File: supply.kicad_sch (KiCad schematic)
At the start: 94 parts, among them J12 PJ-102A, Q12 BSS138W-7-F, Q13 BCM857BS-7-F, Q14 BCM857BS-7-F, Q15 SSM3J332R, Q16 SSM3J332R, Q17 BSS138W-7-F, Q18 BSS138W-7-F, Q19 BSS138W-7-F, Q20 BSS138W-7-F, SW1 PCM12SMTR, U35 RB521S30T1G, U36 RB521S30T1G, U37 74LVC2G14GV, U38 74LVC1G175GV, U39 MP2386GG-P, U40 MP2386GG-P, U41 TPS7B8133DRVR, U42 TPS7A0518PDBVT

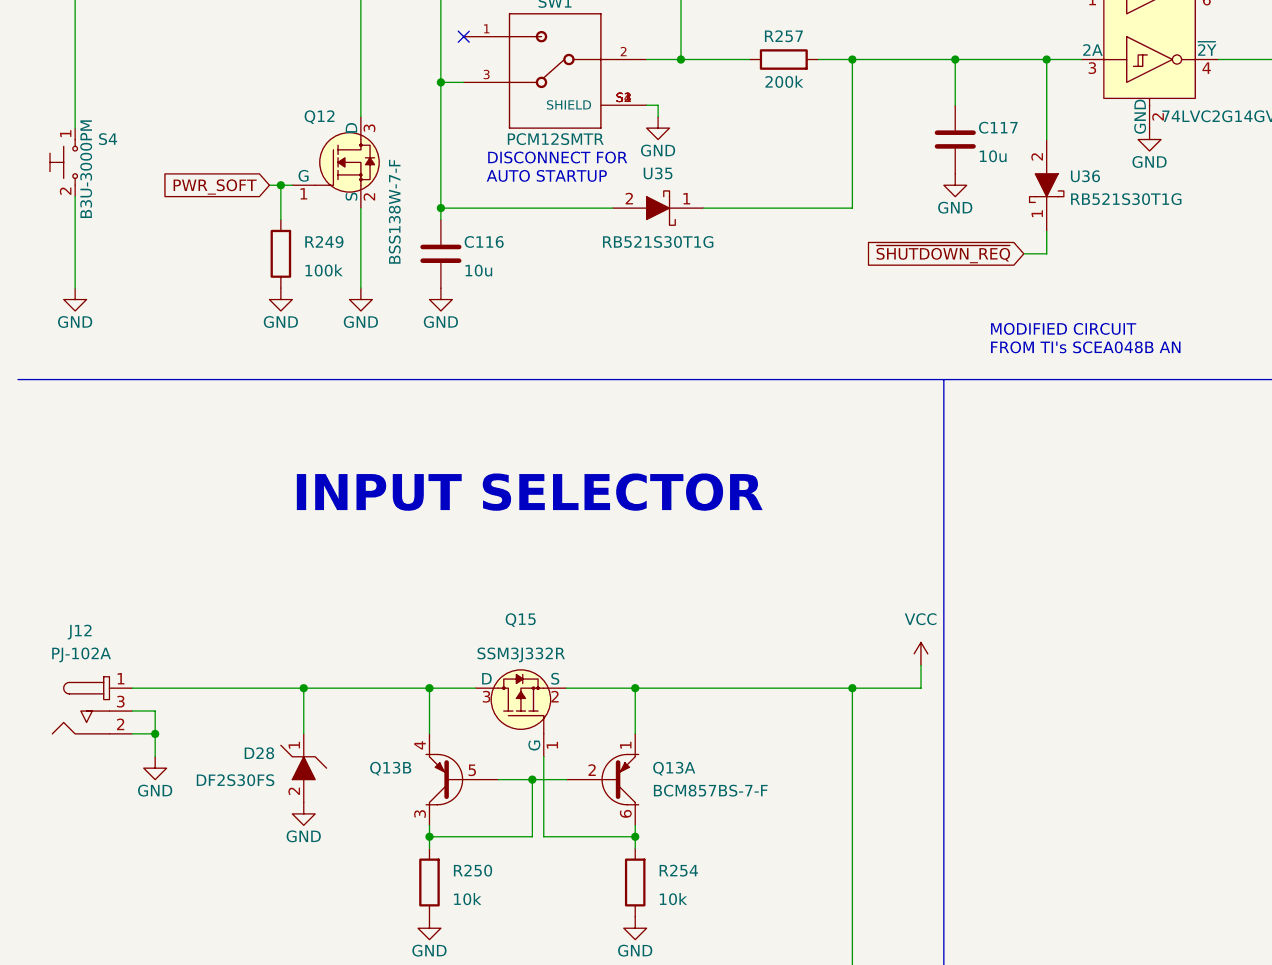
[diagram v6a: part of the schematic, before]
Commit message: Update RB521S30T1G symbol and footprint
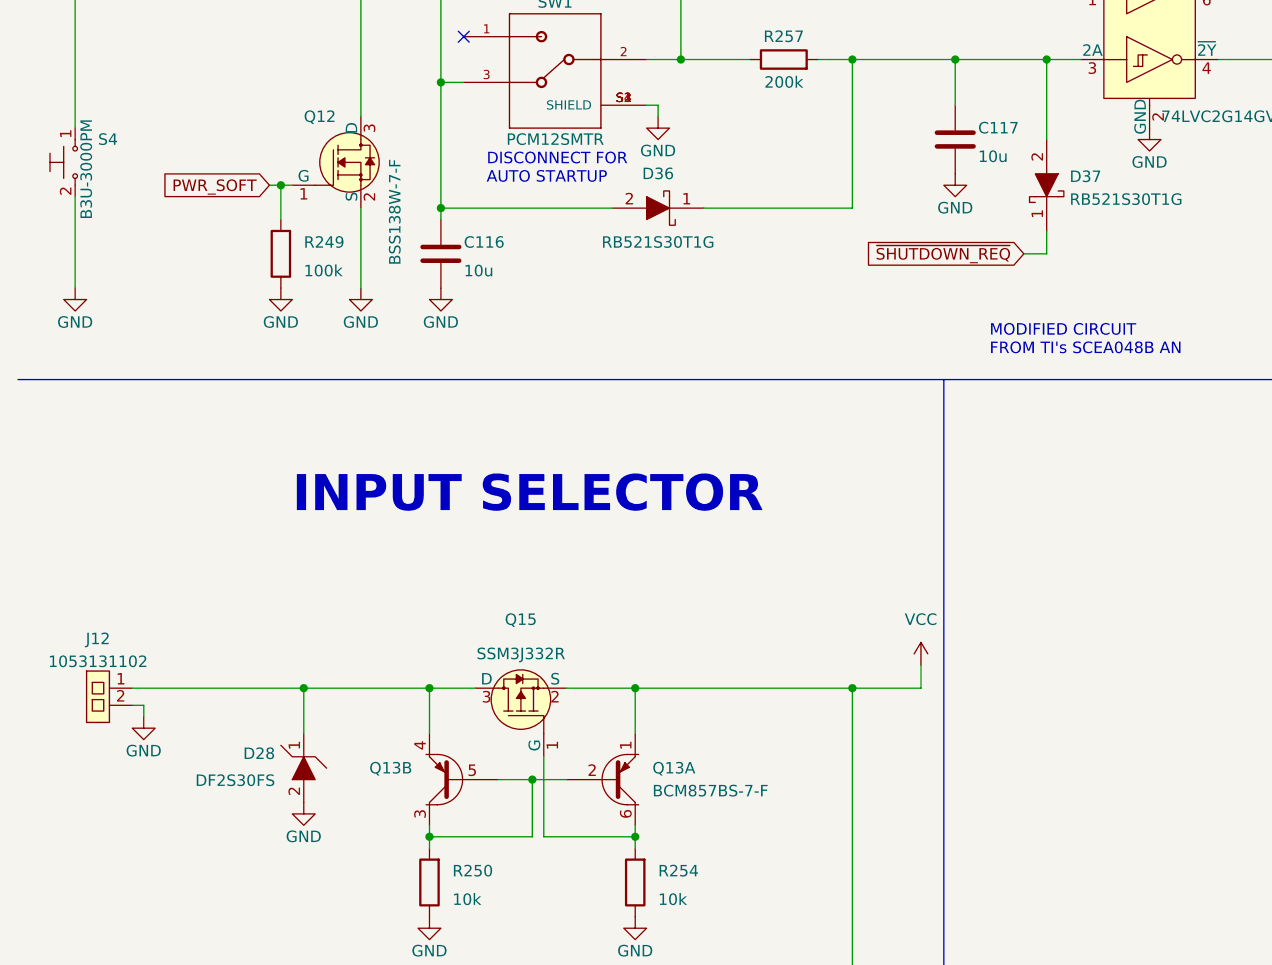
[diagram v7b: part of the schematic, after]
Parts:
- removed J12: PJ-102A, antmicro-footprints:Barrel_Jack_5.5mmODx2.1mmID_PJ-102A, symbol antmicroBarrelPowerConnectors:PJ-102A
- added J12: 1053131102, antmicro-footprints:1053131102, symbol antmicroRectangularConnectorsHeadersFemalePins:1053131102
- renumbered U35 to D36, U36 to D37
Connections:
- net GND: now also J12.2
- net at D28.1, Q13.4, Q15.3 (D): now also J12.1
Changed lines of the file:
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@@
   (junction (at 249.555 127) (diameter 0) (color 0 0 0 0)
   )
-  (junction (at 27.94 134.62) (diameter 0) (color 0 0 0 0)
-  )
   (junction (at 363.855 139.7) (diameter 0) (color 0 0 0 0)
   )
@@
     (stroke (width 0) (type default) (color 0 0 0 0))
   )
-  (wire (pts (xy 27.94 132.08) (xy 27.94 134.62))
-    (stroke (width 0) (type default) (color 0 0 0 0))
-  )
   (wire (pts (xy 86.36 46.99) (xy 86.36 59.69))
     (stroke (width 0) (type default) (color 0 0 0 0))
@@
     (stroke (width 0) (type default) (color 0 0 0 0))
   )
-  (wire (pts (xy 25.4 132.08) (xy 27.94 132.08))
+  (wire (pts (xy 25.4 131.445) (xy 26.67 131.445))
     (stroke (width 0) (type default) (color 0 0 0 0))
   )
@@
     (stroke (width 0) (type default) (color 0 0 0 0))
   )
-  (wire (pts (xy 27.94 134.62) (xy 25.4 134.62))
-    (stroke (width 0) (type default) (color 0 0 0 0))
-  )
   (wire (pts (xy 236.22 127) (xy 249.555 127))
     (stroke (width 0) (type default) (color 0 0 0 0))
@@
     (stroke (width 0) (type default) (color 0 0 0 0))
   )
-  (wire (pts (xy 27.94 134.62) (xy 27.94 137.16))
+  (wire (pts (xy 26.67 131.445) (xy 26.67 132.715))
     (stroke (width 0) (type default) (color 0 0 0 0))
   )
@@
     (pin "6")
   )
-  (symbol (lib_id "antmicroDiodesRectifiersSingle:RB521S30T1G") (at 127 73.66 270) (unit 1)
+  (symbol (lib_name "RB521S30T1G_1") (lib_id "antmicroDiodesRectifiersSingle:RB521S30T1G") (at 127 73.66 270) (unit 1)
     (in_bom yes) (on_board yes) (fields_autoplaced)
-    (property "Reference" "U36" (id 0) (at 129.54 72.7074 90)
+    (property "Reference" "D37" (id 0) (at 129.54 72.7074 90)
       (effects (font (size 1.27 1.27)) (justify left))
     )
@@
   (symbol (lib_id "antmicroDiodesRectifiersSingle:RB521S30T1G") (at 83.82 76.2 0) (unit 1)
     (in_bom yes) (on_board yes)
-    (property "Reference" "U35" (id 0) (at 83.82 72.39 0))
+    (property "Reference" "D36" (id 0) (at 83.82 72.39 0))
     (property "Value" "RB521S30T1G" (id 1) (at 83.82 80.01 0))
     (property "Footprint" "antmicro-footprints:SOD-523" (id 2) (at 86.36 83.82 0)
@@
     (pin "2")
   )
-  (symbol (lib_id "power:GND") (at 27.94 137.16 0) (unit 1)
+  (symbol (lib_id "power:GND") (at 26.67 132.715 0) (unit 1)
     (in_bom yes) (on_board yes)
-    (property "Reference" "#PWR0250" (id 0) (at 27.94 143.51 0)
+    (property "Reference" "#PWR0250" (id 0) (at 26.67 139.065 0)
       (effects (font (size 1.27 1.27)) hide)
     )
-    (property "Value" "GND" (id 1) (at 27.94 140.97 0))
-    (property "Footprint" "" (id 2) (at 27.94 137.16 0)
+    (property "Value" "GND" (id 1) (at 26.67 136.525 0))
+    (property "Footprint" "" (id 2) (at 26.67 132.715 0)
       (effects (font (size 1.27 1.27)) hide)
     )
-    (property "Datasheet" "" (id 3) (at 27.94 137.16 0)
+    (property "Datasheet" "" (id 3) (at 26.67 132.715 0)
       (effects (font (size 1.27 1.27)) hide)
     )
@@
     (pin "1")
   )
-  (symbol (lib_id "antmicroBarrelPowerConnectors:PJ-102A") (at 22.86 129.54 0) (unit 1)
-    (in_bom yes) (on_board yes) (fields_autoplaced)
-    (property "Reference" "J12" (id 0) (at 19.685 123.19 0))
-    (property "Value" "PJ-102A" (id 1) (at 19.685 125.73 0))
-    (property "Footprint" "antmicro-footprints:Barrel_Jack_5.5mmODx2.1mmID_PJ-102A" (id 2) (at 27.94 124.46 0)
-      (effects (font (size 1.524 1.524)) (justify left) hide)
-    )
-    (property "Datasheet" "https://www.cui.com/product/resource/digikeypdf/pj-102a.pdf" (id 3) (at 27.94 121.92 0)
-      (effects (font (size 1.524 1.524)) (justify left) hide)
-    )
-    (property "Manufacturer" "CUI Inc." (id 4) (at 27.94 101.6 0)
-      (effects (font (size 1.524 1.524)) (justify left) hide)
-    )
-    (property "MPN" "PJ-102A" (id 5) (at 27.94 116.84 0)
-      (effects (font (size 1.524 1.524)) (justify left) hide)
-    )
-    (pin "1")
-    (pin "2")
-    (pin "3")
-  )
   (symbol (lib_id "antmicroCapacitorsmisc:C_22u_0805_25V") (at 222.885 132.08 0) (unit 1)
     (in_bom yes) (on_board yes) (fields_autoplaced)
@@
     )
     (pin "1")
+    (pin "2")
+  )
+  (symbol (lib_id "antmicroRectangularConnectorsHeadersFemalePins:1053131102") (at 20.32 127.635 0) (unit 1)
+    (in_bom yes) (on_board yes) (fields_autoplaced)
+    (property "Reference" "J12" (id 0) (at 21.59 124.0622 0))
+    (property "Value" "1053131102" (id 1) (at 21.59 126.5991 0))
+    (property "Footprint" "antmicro-footprints:1053131102" (id 2) (at 15.875 135.89 0)
+      (effects (font (size 1.27 1.27)) hide)
+    )
+    (property "Datasheet" "" (id 3) (at 20.32 127.635 0)
+      (effects (font (size 1.27 1.27)) hide)
+    )
+    (property "Manufacturer" "Molex" (id 4) (at 19.05 140.97 0)
+      (effects (font (size 1.27 1.27)) hide)
+    )
+    (property "MPN" "1053131102" (id 5) (at 17.145 139.065 0)
+      (effects (font (size 1.27 1.27)) hide)
+    )
+    (pin "1")

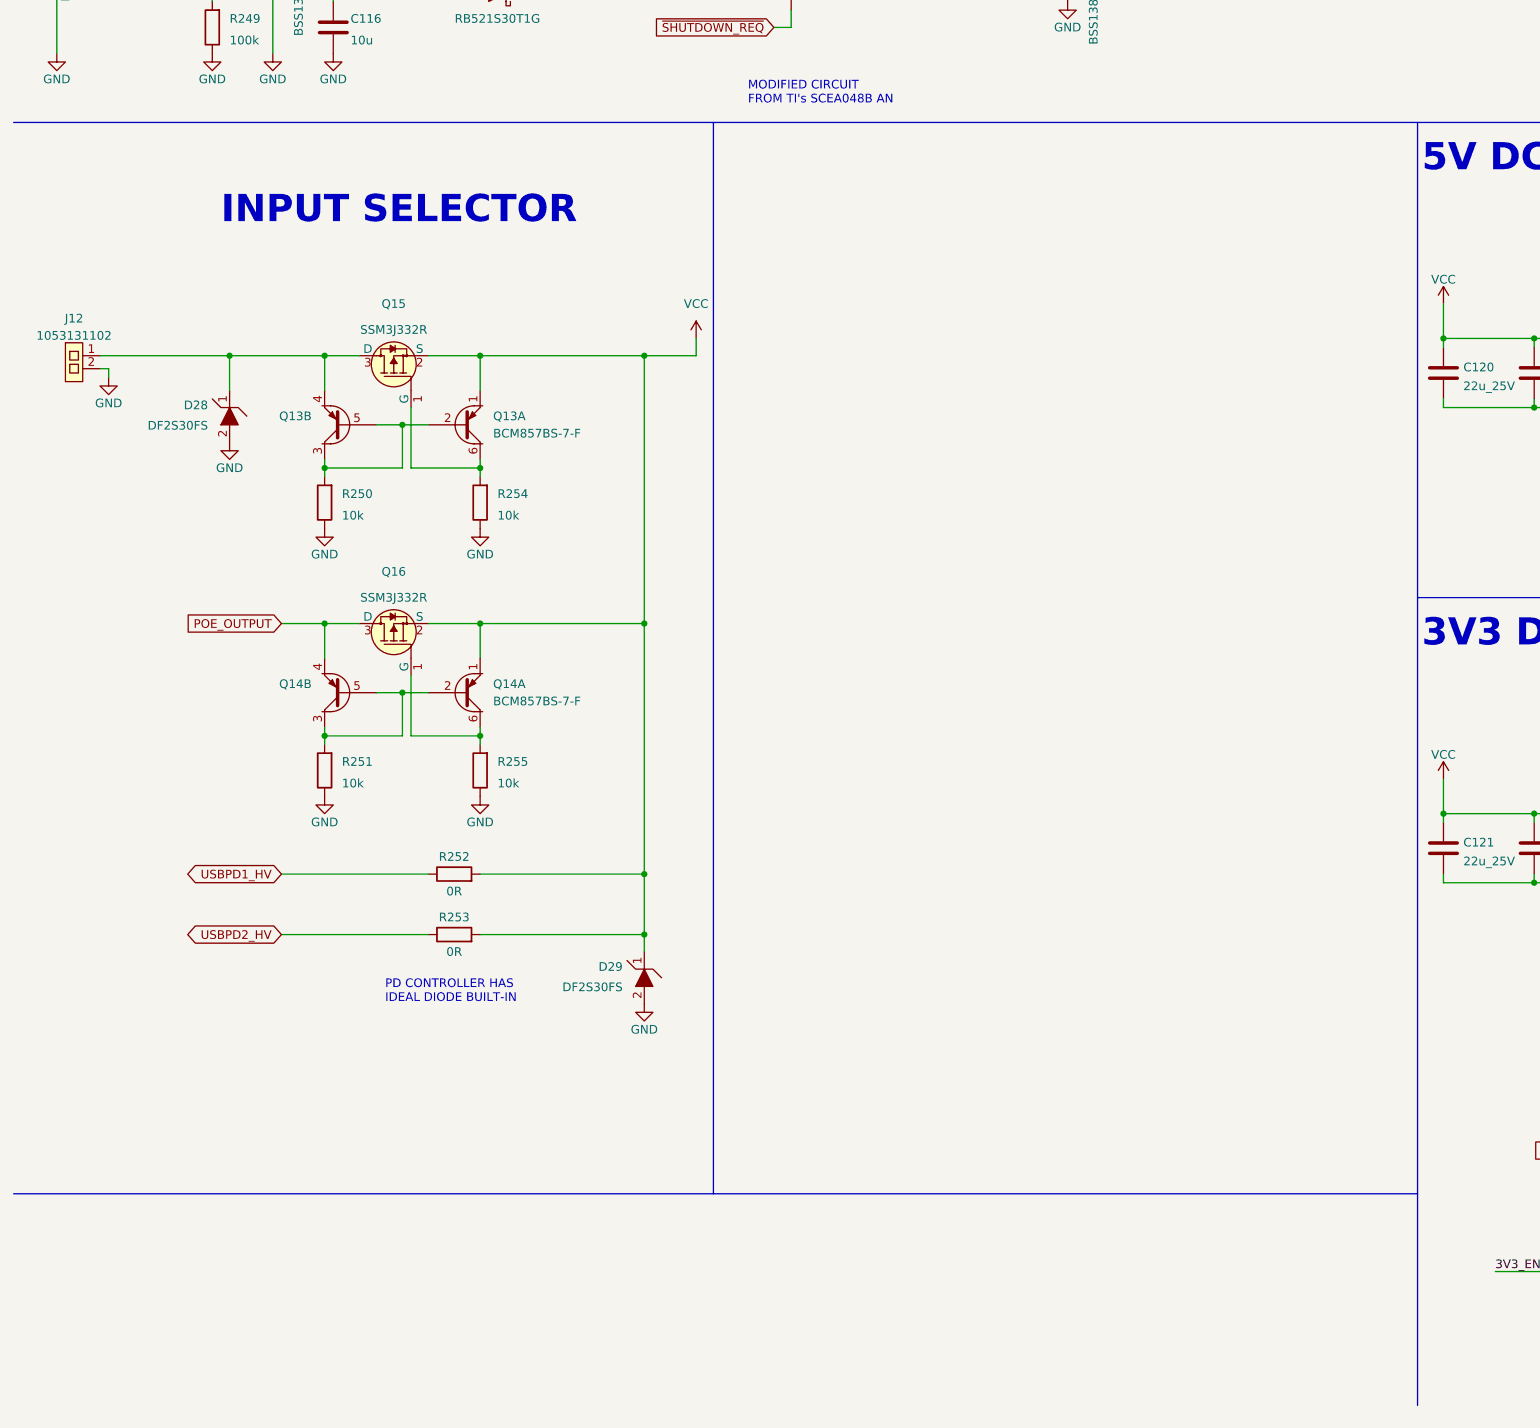
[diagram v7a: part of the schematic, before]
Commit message: Added power switch and soft start circuitry
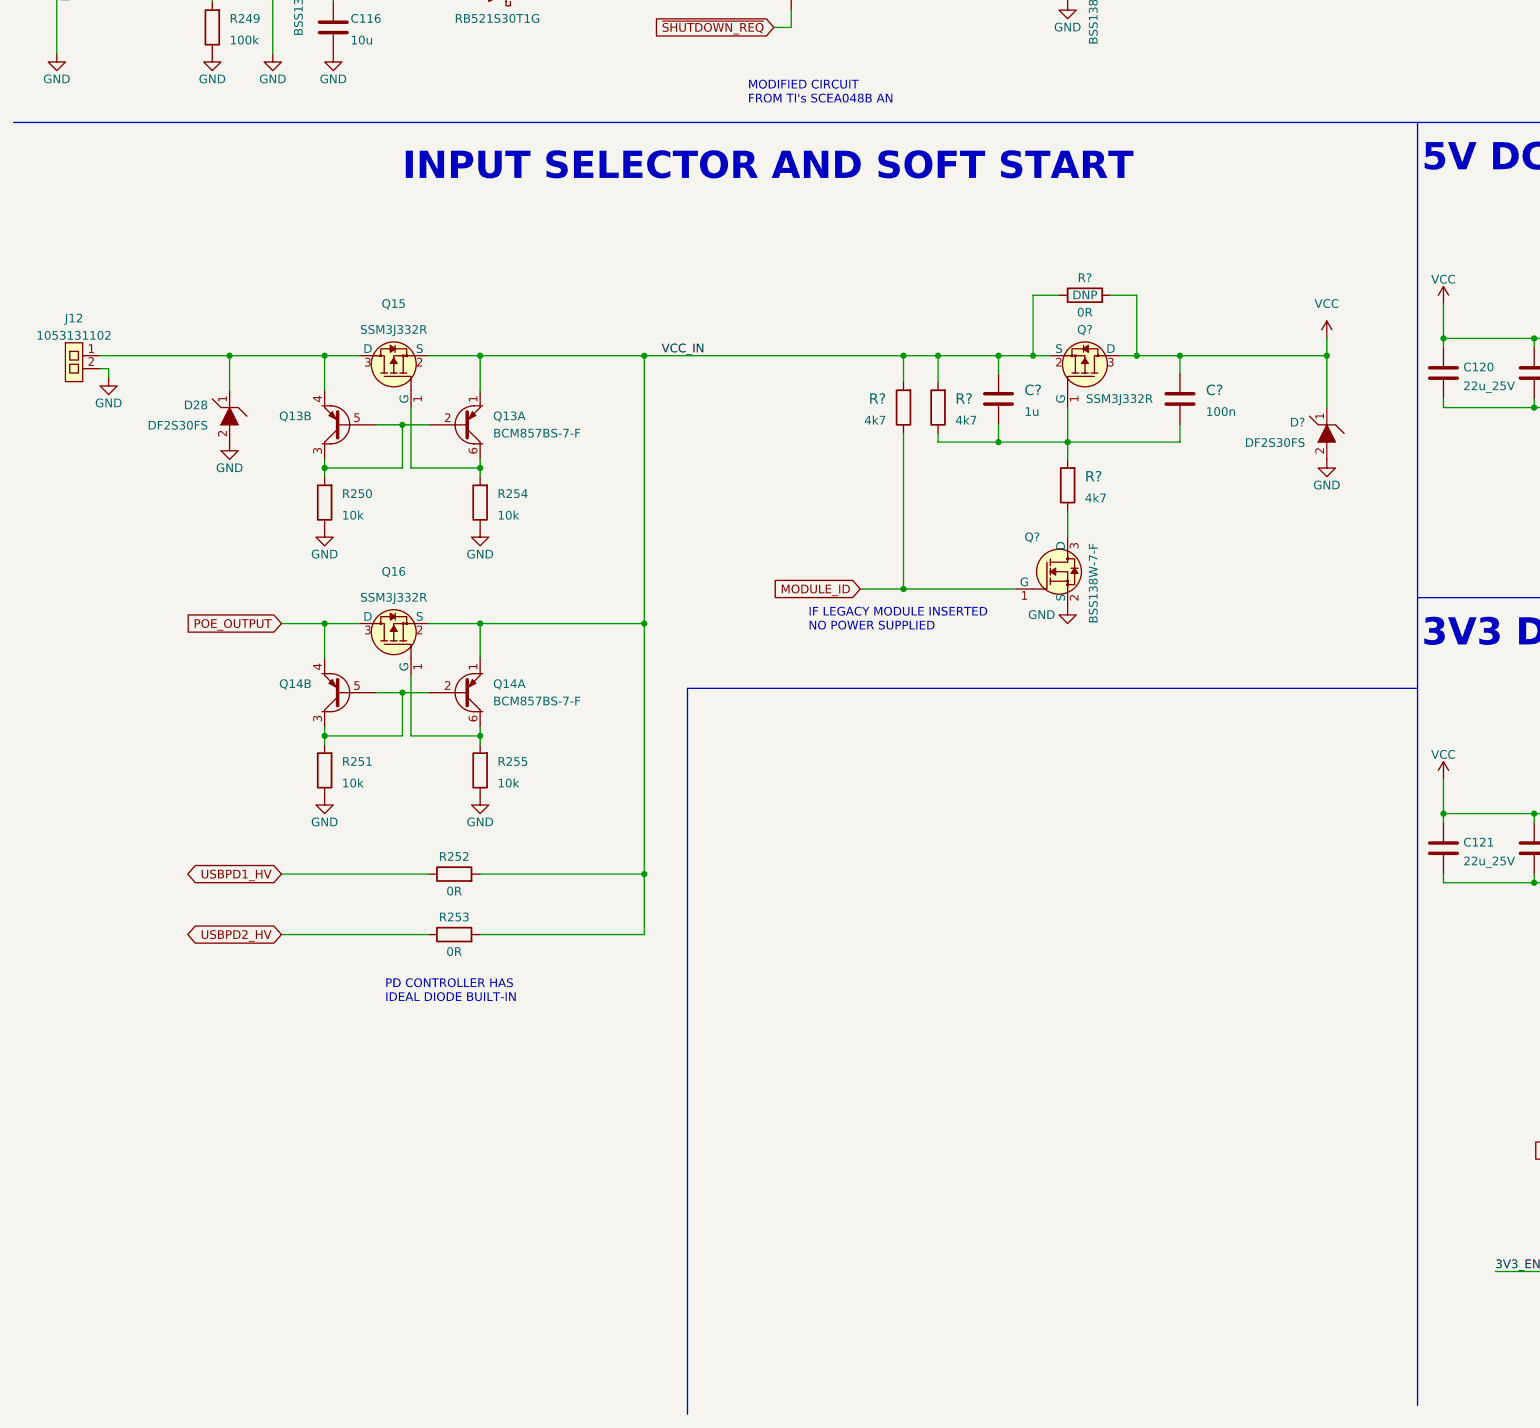
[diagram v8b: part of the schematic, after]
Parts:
- removed D29: DF2S30FS, antmicro-footprints:SOD-923, symbol antmicroTVSDiodes:DF2S30FS
- added C?: C_1u_0402, antmicro-footprints:0402-cap, symbol antmicroCapacitors0402:C_1u_0402
- added C?: C_100n_0402, antmicro-footprints:0402-cap, symbol antmicroCapacitors0402:C_100n_0402
- added D?: DF2S30FS, antmicro-footprints:SOD-923, symbol antmicroTVSDiodes:DF2S30FS
- added Q?: BSS138W-7-F, antmicro-footprints:SOT-323, symbol antmicroTransistorsFETsMOSFETsSingle:BSS138W-7-F
- added Q?: SSM3J332R, antmicro-footprints:SOT-23-3, symbol antmicroTransistorsFETsMOSFETsSingle:SSM3J332R
- added R? (x3): R_4k7_0402, antmicro-footprints:0402-res, symbol antmicroResistors0402:R_4k7_0402
- added R?: R_0R_1206, antmicro-footprints:1206-res, symbol antmicroResistorsmisc:R_0R_1206
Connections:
- net GND: now also D?.2, Q?.2 (S)
- net VCC: now also C?.1, D?.1, Q?.3 (D), R?.2; no longer Q13.1, Q14.1, Q15.2 (S), Q16.2 (S), R252.2, R253.2
- new net: C?.2, C?.2, Q?.1 (G), R?.1, R?.2
- new net: Q?.3 (D), R?.1
- new net MODULE_ID: Q?.1 (G), R?.1
- new net VCC_IN: C?.1, Q13.1, Q14.1, Q15.2 (S), Q16.2 (S), Q?.2 (S), R252.2, R253.2, R?.1, R?.2, R?.2
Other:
- note added: "IF LEGACY MODULE INSERTED NO POWER SUPPLIED"
- note added: "INPUT SELECTOR AND SOFT START"
- note removed: "INPUT SELECTOR"
